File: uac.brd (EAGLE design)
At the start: 100 x 100 mm, 201 parts, among them Q1 2N7002CK4SST, Q6 2N7002CK4SST, Q7 2N7002CK4SST, U2 ADXL345, Y1 RESONATORSMD

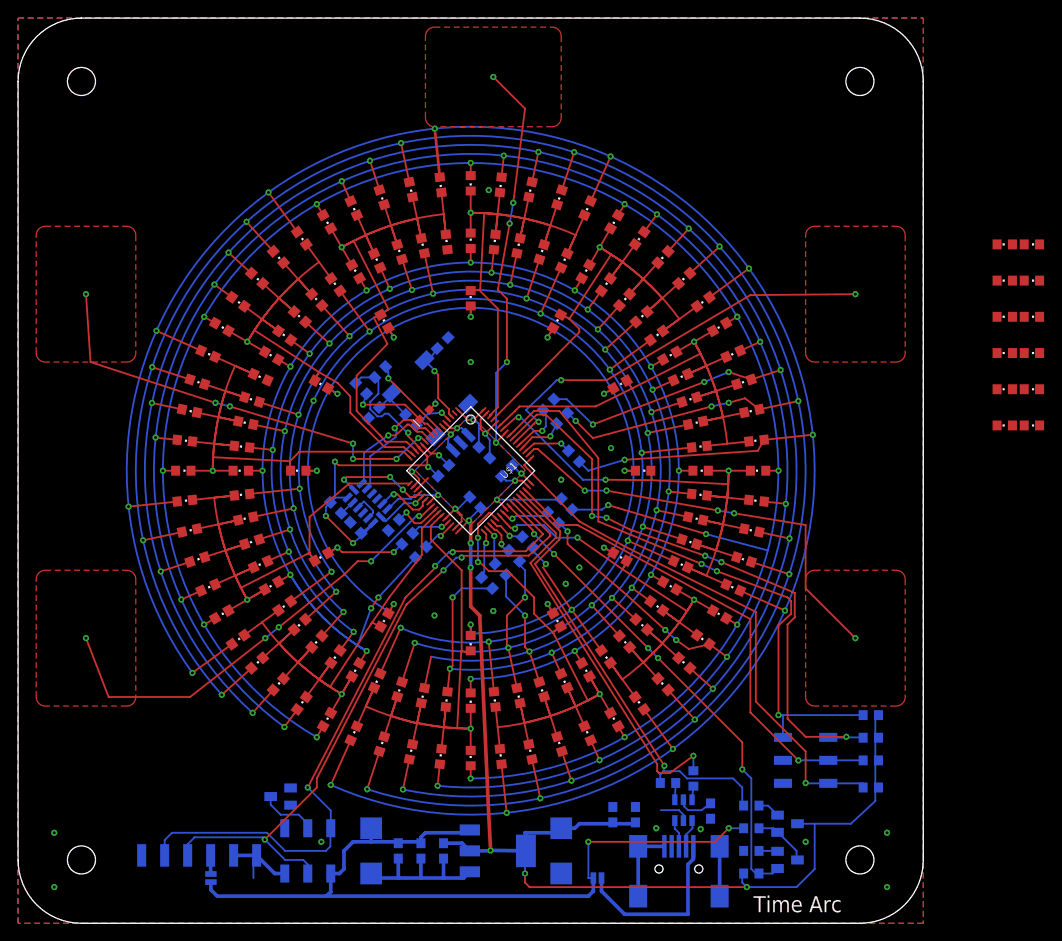
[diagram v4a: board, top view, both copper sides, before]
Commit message: connected wake
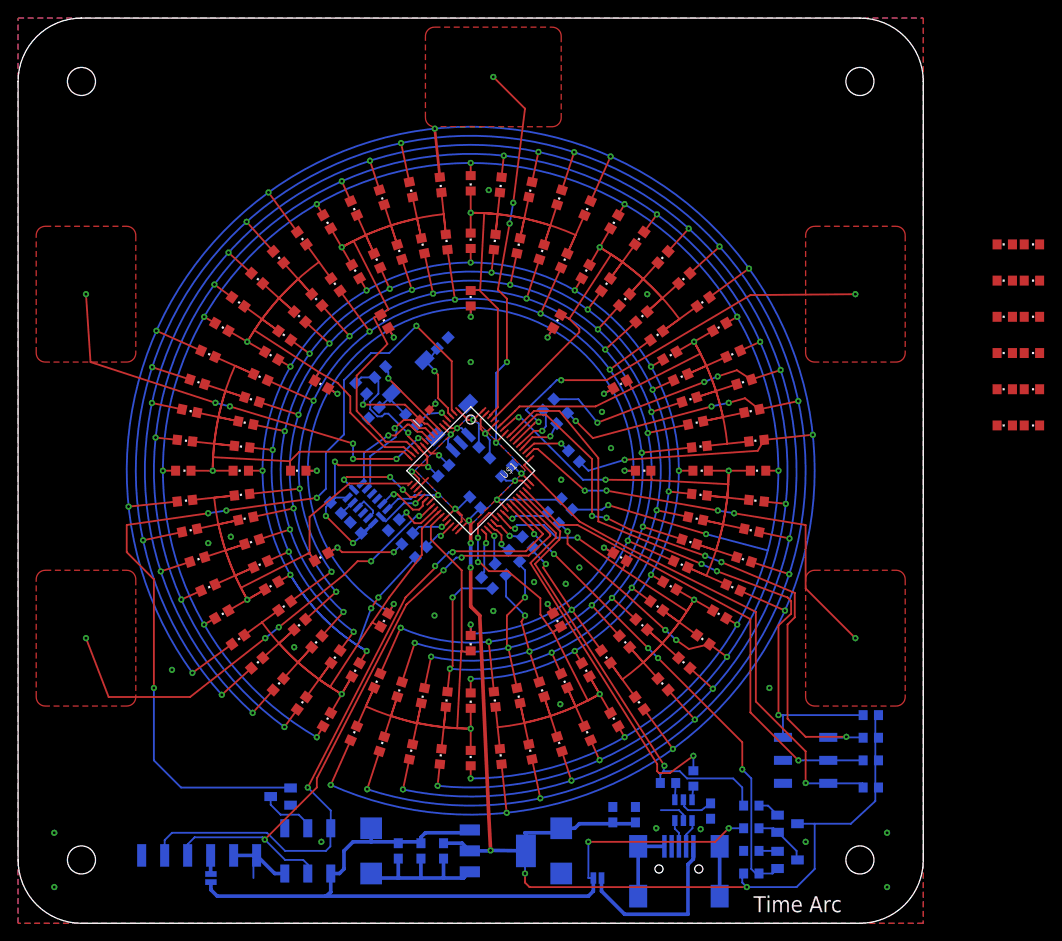
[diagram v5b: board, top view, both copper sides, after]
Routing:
- net WAKE: track 0.00 -> 100.9 mm, vias 0 -> 5
- net DOZEN6: track 73.9 -> 85.1 mm, vias 12 -> 13
- net DOZEN4: vias 12 -> 13
- net GND: vias 22 -> 31
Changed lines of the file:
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@@
 <wire x1="53.90104375" y1="36.09895625" x2="56" y2="34" width="0.2032" layer="16"/>
 <via x="56" y="34" extent="1-16" drill="0.31"/>
-<wire x1="56" y1="34" x2="56" y2="30.51716875" width="0.2032" layer="1"/>
-<wire x1="56" y1="30.51716875" x2="56.489359375" y2="30.027809375" width="0.2032" layer="1"/>
+<wire x1="56" y1="34" x2="55.6" y2="33.31716875" width="0.2032" layer="1"/>
+<wire x1="55.6" y1="33.31716875" x2="56.489359375" y2="30.027809375" width="0.2032" layer="1"/>
+<via x="45.63" y="29.46" extent="1-16" drill="0.31"/>
 <wire x1="69.972190625" y1="56.489359375" x2="64.051740625" y2="65.606040625" width="0" layer="19" extent="1-1"/>
 <wire x1="54.36615" y1="70.5411" x2="64.051740625" y2="65.606040625" width="0" layer="19" extent="1-1"/>
@@
 <wire x1="65.606040625" y1="35.948259375" x2="70.5411" y2="45.63385" width="0" layer="19" extent="1-1"/>
 <wire x1="56" y1="34" x2="65.606040625" y2="35.948259375" width="0" layer="19" extent="16-16"/>
-<wire x1="45.63385" y1="29.4589" x2="56" y2="30.51716875" width="0" layer="19" extent="1-1"/>
-<wire x1="45.633853125" y1="29.4589" x2="45.63385" y2="29.4589" width="0" layer="19" extent="1-16"/>
+<wire x1="45.63" y1="29.46" x2="53.90104375" y2="36.09895625" width="0" layer="19" extent="16-16"/>
+<wire x1="45.63385" y1="29.4589" x2="45.63" y2="29.46" width="0" layer="19" extent="1-1"/>
+<wire x1="45.633853125" y1="29.4589" x2="45.63" y2="29.46" width="0" layer="19" extent="16-16"/>
 <wire x1="34.393959375" y1="64.051740625" x2="43.510640625" y2="69.972190625" width="0" layer="19" extent="1-1"/>
 <wire x1="29.4589" y1="54.36615" x2="34.393959375" y2="64.051740625" width="0" layer="19" extent="1-1"/>
@@
 <wire x1="58" y1="39.3" x2="61" y2="34.7966" width="0.2032" layer="1"/>
 <wire x1="61" y1="34.7966" x2="61.16791875" y2="34.62868125" width="0.2032" layer="1"/>
+<wire x1="47.433834375" y1="74.415515625" x2="48.26" y2="68.9" width="0.2032" layer="1"/>
+<via x="48.26" y="68.9" extent="1-16" drill="0.31"/>
+<wire x1="48.26" y1="68.9" x2="48.1" y2="68.9" width="0.2032" layer="16"/>
+<wire x1="27.57246875" y1="59.985390625" x2="32.642640625" y2="57.728" width="0.2032" layer="1"/>
 <wire x1="57.728" y1="67.357359375" x2="65.37131875" y2="61.16791875" width="0" layer="19" extent="1-1"/>
+<wire x1="48.26" y1="68.9" x2="57.728" y2="67.357359375" width="0" layer="19" extent="1-1"/>
 <wire x1="68.89591875" y1="51.986040625" x2="65.37131875" y2="61.16791875" width="0" layer="19" extent="1-1"/>
 <wire x1="67.357359375" y1="42.272" x2="68.89591875" y2="51.986040625" width="0" layer="19" extent="1-1"/>
@@
 <wire x1="31.10408125" y1="48.013959375" x2="34.62868125" y2="38.83208125" width="0" layer="19" extent="16-16"/>
 <wire x1="32.642640625" y1="57.728" x2="31.10408125" y2="48.013959375" width="0" layer="19" extent="1-1"/>
-<wire x1="27.57246875" y1="59.985390625" x2="32.642640625" y2="57.728" width="0" layer="19" extent="1-1"/>
 <wire x1="38.83208125" y1="65.37131875" x2="32.642640625" y2="57.728" width="0" layer="19" extent="1-1"/>
-<wire x1="47.433834375" y1="74.415515625" x2="57.728" y2="67.357359375" width="0" layer="19" extent="1-1"/>
 </signal>
 <signal name="DOZEN7">
@@
 <via x="61.124609375" y="15.76196875" extent="1-16" drill="0.31"/>
 <wire x1="60.073946875" y1="18.995546875" x2="61.124609375" y2="15.76196875" width="0.2032" layer="1"/>
-<wire x1="59.20104375" y1="57.901040625" x2="60.6" y2="57.9" width="0.2032" layer="16"/>
-<wire x1="60.6" y1="57.9" x2="63.5" y2="55.1" width="0.2032" layer="16"/>
-<via x="63.5" y="55.1" extent="1-16" drill="0.31"/>
-<wire x1="63.5" y1="55.1" x2="75.8" y2="59.8" width="0.2032" layer="1"/>
+<wire x1="59.20104375" y1="57.901040625" x2="61.9" y2="57.9" width="0.2032" layer="16"/>
+<wire x1="61.9" y1="57.9" x2="64" y2="55.3" width="0.2032" layer="16"/>
+<via x="64" y="55.3" extent="1-16" drill="0.31"/>
+<wire x1="64" y1="55.3" x2="75.8" y2="59.8" width="0.2032" layer="1"/>
 <via x="75.8" y="59.8" extent="1-16" drill="0.31"/>
-<wire x1="75.8" y1="59.8" x2="78.5" y2="60.9" width="0.2032" layer="16"/>
-<via x="78.5" y="60.9" extent="1-16" drill="0.31"/>
-<wire x1="78.5" y1="60.9" x2="81.00445" y2="60.073946875" width="0.2032" layer="1"/>
-<wire x1="78.5" y1="60.9" x2="71.81365" y2="74.22651875" width="0" layer="19" extent="1-1"/>
+<wire x1="75.8" y1="59.8" x2="77.29" y2="60.41" width="0.2032" layer="16"/>
+<via x="77.29" y="60.41" extent="1-16" drill="0.31"/>
+<wire x1="77.29" y1="60.41" x2="79.4" y2="61.1" width="0.2032" layer="1"/>
+<wire x1="79.4" y1="61.1" x2="81.00445" y2="60.073946875" width="0.2032" layer="1"/>
+<wire x1="77.29" y1="60.41" x2="71.81365" y2="74.22651875" width="0" layer="19" extent="1-1"/>
 <wire x1="56.777928125" y1="81.887625" x2="71.81365" y2="74.22651875" width="0" layer="19" extent="1-1"/>
 <wire x1="81.887625" y1="43.22206875" x2="81.00445" y2="60.073946875" width="0" layer="19" extent="1-1"/>
@@
 <wire x1="51" y1="39.9" x2="52" y2="38.9" width="0.2032" layer="1"/>
 <wire x1="52" y1="38.9" x2="54.1" y2="38.9" width="0.2032" layer="1"/>
-<wire x1="54.1" y1="38.9" x2="57" y2="36" width="0.2032" layer="1"/>
-<wire x1="57" y1="36" x2="57" y2="34.205475" width="0.2032" layer="1"/>
-<wire x1="57" y1="34.205475" x2="59.13611875" y2="32.06935625" width="0.2032" layer="1"/>
+<wire x1="54.1" y1="38.9" x2="57.7" y2="35.9" width="0.2032" layer="1"/>
+<wire x1="57.7" y1="35.9" x2="57.7" y2="34.105475" width="0.2032" layer="1"/>
+<wire x1="57.7" y1="34.105475" x2="59.13611875" y2="32.06935625" width="0.2032" layer="1"/>
 <wire x1="52.828425" y1="44.696696875" x2="112.85" y2="75" width="0" layer="19" extent="1-1"/>
 </signal>
@@
 <via x="62" y="39.3" extent="1-16" drill="0.31"/>
 <via x="60.5" y="37.5" extent="1-16" drill="0.31"/>
+<via x="83" y="26" extent="1-16" drill="0.31"/>
+<via x="17" y="28" extent="1-16" drill="0.31"/>
+<via x="21" y="42" extent="1-16" drill="0.31"/>
+<via x="23.5" y="42.7" extent="1-16" drill="0.31"/>
+<via x="30.5" y="30.5" extent="1-16" drill="0.31"/>
+<via x="69.5" y="69.5" extent="1-16" drill="0.31"/>
+<via x="64.5" y="56.5" extent="1-16" drill="0.31"/>
+<via x="59.9" y="24.2" extent="1-16" drill="0.31"/>
+<via x="57" y="37.7" extent="1-16" drill="0.31"/>
 <wire x1="39.2" y1="45.6" x2="43.6360375" y2="48.23223125" width="0" layer="19" extent="1-16"/>
-<wire x1="60.5" y1="37.5" x2="52.5" y2="34.5" width="0" layer="19" extent="1-1"/>
+<wire x1="57" y1="37.7" x2="52.5" y2="34.5" width="0" layer="19" extent="1-1"/>
+<wire x1="38.698959375" y1="55.79895625" x2="44.671571875" y2="52.828428125" width="0" layer="19" extent="1-16"/>
 </signal>
 <signal name="+3V3">
@@
 <wire x1="45.39063125" y1="62.207284375" x2="46.298959375" y2="63.49895625" width="0.2032" layer="16"/>
 <wire x1="47.878678125" y1="56.01040625" x2="47.878678125" y2="56.021321875" width="0.2032" layer="1"/>
-<wire x1="47.878678125" y1="56.021321875" x2="47.6" y2="56.3" width="0.2032" layer="1"/>
-<wire x1="47.6" y1="56.3" x2="47.6" y2="56.8" width="0.2032" layer="1"/>
-<wire x1="47.6" y1="56.8" x2="46.4" y2="58" width="0.2032" layer="1"/>
+<wire x1="47.878678125" y1="56.021321875" x2="47.5" y2="56.4" width="0.2032" layer="1"/>
+<wire x1="47.5" y1="56.4" x2="47.5" y2="56.9" width="0.2032" layer="1"/>
+<wire x1="47.5" y1="56.9" x2="46.4" y2="58" width="0.2032" layer="1"/>
 <wire x1="46.4" y1="58" x2="46.4" y2="60.6" width="0.2032" layer="1"/>
 <wire x1="46.4" y1="60.6" x2="46" y2="61" width="0.2032" layer="1"/>
@@
 <contactref element="Q1" pad="1"/>
 <contactref element="U$1" pad="2"/>
-<wire x1="30.1" y1="14.95" x2="48.23223125" y2="56.363959375" width="0" layer="19" extent="1-16"/>
+<wire x1="48.23223125" y1="56.363959375" x2="48.23223125" y2="56.36776875" width="0.2032" layer="1"/>
+<wire x1="48.23223125" y1="56.36776875" x2="47.9" y2="56.7" width="0.2032" layer="1"/>
+<wire x1="47.9" y1="56.7" x2="47.9" y2="62.1" width="0.2032" layer="1"/>
+<wire x1="47.9" y1="62.1" x2="44" y2="66" width="0.2032" layer="1"/>
+<via x="44" y="66" extent="1-16" drill="0.31"/>
+<wire x1="44" y1="66" x2="41" y2="63" width="0.2032" layer="16"/>
+<wire x1="41" y1="63" x2="39" y2="63" width="0.2032" layer="16"/>
+<wire x1="39" y1="63" x2="36" y2="60" width="0.2032" layer="16"/>
+<wire x1="36" y1="60" x2="36" y2="54" width="0.2032" layer="16"/>
+<wire x1="36" y1="54" x2="34" y2="52" width="0.2032" layer="16"/>
+<wire x1="34" y1="52" x2="34" y2="48" width="0.2032" layer="16"/>
+<wire x1="34" y1="48" x2="33" y2="47" width="0.2032" layer="16"/>
+<via x="33" y="47" extent="1-16" drill="0.31"/>
+<wire x1="33" y1="47" x2="23" y2="45.6" width="0.2032" layer="1"/>
+<via x="23" y="45.6" extent="1-16" drill="0.31"/>
+<wire x1="23" y1="45.6" x2="21" y2="45.3" width="0.2032" layer="16"/>
+<via x="21" y="45.3" extent="1-16" drill="0.31"/>
+<wire x1="21" y1="45.3" x2="12" y2="44" width="0.2032" layer="1"/>
+<wire x1="12" y1="44" x2="12" y2="41" width="0.2032" layer="1"/>
+<wire x1="12" y1="41" x2="15" y2="38" width="0.2032" layer="1"/>
+<wire x1="15" y1="38" x2="15" y2="26" width="0.2032" layer="1"/>
+<via x="15" y="26" extent="1-16" drill="0.31"/>
+<wire x1="15" y1="26" x2="15" y2="18" width="0.2032" layer="16"/>
+<wire x1="15" y1="18" x2="18" y2="15" width="0.2032" layer="16"/>
+<wire x1="18" y1="15" x2="30.05" y2="15" width="0.2032" layer="16"/>
+<wire x1="30.05" y1="15" x2="30.1" y2="14.95" width="0.2032" layer="16"/>
 </signal>
 <signal name="TOUCH1">

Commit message: placing specials
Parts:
- moved SPECIAL3 76.7 mm to (33.0, 53.0)
- moved SPECIAL4 76.1 mm to (33.0, 56.0)
- moved SPECIAL5 70.6 mm to (38.5, 59.5), turned to 180 degrees
- moved SPECIAL6 60.7 mm to (51.5, 59.5), turned to 180 degrees
- moved SPECIAL7 58.0 mm to (54.0, 59.5), turned to 180 degrees
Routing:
- net DOZEN7: track 56.9 -> 58.2 mm
- net ARCDOZEN_6: track 85.4 -> 86.6 mm
- net ARCDOZEN_8: track 79.6 -> 80.4 mm
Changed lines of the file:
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@@
 <attribute name="VALUE" x="110" y="69" size="0.8128" layer="27" font="vector" rot="R180"/>
 </element>
-<element name="SPECIAL3" library="Custom components" package="CHIPLED_0603" value="" x="109" y="63" smashed="yes" rot="R90">
-<attribute name="NAME" x="110" y="62" size="0.8128" layer="51" font="vector" rot="R180"/>
-<attribute name="VALUE" x="110" y="65" size="0.8128" layer="27" font="vector" rot="R180"/>
-</element>
-<element name="SPECIAL4" library="Custom components" package="CHIPLED_0603" value="" x="109" y="59" smashed="yes" rot="R90">
-<attribute name="NAME" x="110" y="58" size="0.8128" layer="51" font="vector" rot="R180"/>
-<attribute name="VALUE" x="110" y="61" size="0.8128" layer="27" font="vector" rot="R180"/>
-</element>
-<element name="SPECIAL5" library="Custom components" package="CHIPLED_0603" value="" x="109" y="55" smashed="yes" rot="R90">
-<attribute name="NAME" x="110" y="54" size="0.8128" layer="51" font="vector" rot="R180"/>
-<attribute name="VALUE" x="110" y="57" size="0.8128" layer="27" font="vector" rot="R180"/>
-</element>
-<element name="SPECIAL6" library="Custom components" package="CHIPLED_0603" value="" x="112" y="55" smashed="yes" rot="R270">
-<attribute name="NAME" x="111" y="56" size="0.8128" layer="51" font="vector"/>
-<attribute name="VALUE" x="111" y="53" size="0.8128" layer="27" font="vector"/>
-</element>
-<element name="SPECIAL7" library="Custom components" package="CHIPLED_0603" value="" x="112" y="59" smashed="yes" rot="R270">
-<attribute name="NAME" x="111" y="60" size="0.8128" layer="51" font="vector"/>
-<attribute name="VALUE" x="111" y="57" size="0.8128" layer="27" font="vector"/>
+<element name="SPECIAL3" library="Custom components" package="CHIPLED_0603" value="" x="33" y="53" smashed="yes" rot="R90">
+<attribute name="NAME" x="34" y="52" size="0.8128" layer="51" font="vector" rot="R180"/>
+<attribute name="VALUE" x="34" y="55" size="0.8128" layer="27" font="vector" rot="R180"/>
+</element>
+<element name="SPECIAL4" library="Custom components" package="CHIPLED_0603" value="" x="33" y="56" smashed="yes" rot="R90">
+<attribute name="NAME" x="34" y="55" size="0.8128" layer="51" font="vector" rot="R180"/>
+<attribute name="VALUE" x="34" y="58" size="0.8128" layer="27" font="vector" rot="R180"/>
+</element>
+<element name="SPECIAL5" library="Custom components" package="CHIPLED_0603" value="" x="38.5" y="59.5" smashed="yes" rot="R180">
+<attribute name="NAME" x="39.5" y="60.5" size="0.8128" layer="51" font="vector" rot="R270"/>
+<attribute name="VALUE" x="36.5" y="60.5" size="0.8128" layer="27" font="vector" rot="R270"/>
+</element>
+<element name="SPECIAL6" library="Custom components" package="CHIPLED_0603" value="" x="51.5" y="59.5" smashed="yes" rot="R180">
+<attribute name="NAME" x="52.5" y="60.5" size="0.8128" layer="51" font="vector" rot="R270"/>
+<attribute name="VALUE" x="49.5" y="60.5" size="0.8128" layer="27" font="vector" rot="R270"/>
+</element>
+<element name="SPECIAL7" library="Custom components" package="CHIPLED_0603" value="" x="54" y="59.5" smashed="yes" rot="R180">
+<attribute name="NAME" x="55" y="60.5" size="0.8128" layer="51" font="vector" rot="R270"/>
+<attribute name="VALUE" x="52" y="60.5" size="0.8128" layer="27" font="vector" rot="R270"/>
 </element>
 <element name="SPECIAL8" library="Custom components" package="CHIPLED_0603" value="" x="112" y="63" smashed="yes" rot="R270">
@@
 <via x="76" y="43" extent="1-16" drill="0.31"/>
 <wire x1="76" y1="43" x2="82.8" y2="41.2" width="0.2032" layer="16"/>
+<wire x1="66.3" y1="21.767565625" x2="67" y2="20.6" width="0.2032" layer="1"/>
 <wire x1="78.23243125" y1="66.3" x2="66.3" y2="78.23243125" width="0" layer="19" extent="1-1"/>
 <wire x1="50" y1="82.6" x2="66.3" y2="78.23243125" width="0" layer="19" extent="1-1"/>
@@
 <wire x1="109.85" y1="67" x2="109.85" y2="71" width="0" layer="19" extent="1-1"/>
 <wire x1="111.15" y1="67" x2="109.85" y2="67" width="0" layer="19" extent="1-1"/>
-<wire x1="109.85" y1="63" x2="109.85" y2="67" width="0" layer="19" extent="1-1"/>
-<wire x1="111.15" y1="63" x2="109.85" y2="63" width="0" layer="19" extent="1-1"/>
-<wire x1="109.85" y1="59" x2="109.85" y2="63" width="0" layer="19" extent="1-1"/>
-<wire x1="111.15" y1="59" x2="109.85" y2="59" width="0" layer="19" extent="1-1"/>
-<wire x1="109.85" y1="55" x2="109.85" y2="59" width="0" layer="19" extent="1-1"/>
-<wire x1="111.15" y1="55" x2="109.85" y2="55" width="0" layer="19" extent="1-1"/>
-<wire x1="40.898959375" y1="43.39895625" x2="109.85" y2="55" width="0" layer="19" extent="1-16"/>
+<wire x1="111.15" y1="63" x2="111.15" y2="67" width="0" layer="19" extent="1-1"/>
+<wire x1="54" y1="60.35" x2="109.85" y2="67" width="0" layer="19" extent="1-1"/>
+<wire x1="51.5" y1="60.35" x2="54" y2="60.35" width="0" layer="19" extent="1-1"/>
+<wire x1="38.5" y1="60.35" x2="51.5" y2="60.35" width="0" layer="19" extent="1-1"/>
+<wire x1="33.85" y1="56" x2="38.5" y2="60.35" width="0" layer="19" extent="1-1"/>
+<wire x1="33.85" y1="53" x2="33.85" y2="56" width="0" layer="19" extent="1-1"/>
+<wire x1="40.898959375" y1="43.39895625" x2="33.85" y2="53" width="0" layer="19" extent="1-16"/>
 </signal>
 <signal name="ARCDOZEN_3">
@@
 <wire x1="42.6" y1="52.1" x2="31.080690625" y2="52.1" width="0.2032" layer="1"/>
 <wire x1="31.080690625" y1="52.1" x2="30.027409375" y2="51.04671875" width="0.2032" layer="1"/>
-<wire x1="43.282484375" y1="51.4142125" x2="108.15" y2="63" width="0" layer="19" extent="1-1"/>
+<wire x1="31.080690625" y1="52.1" x2="32.15" y2="53" width="0" layer="19" extent="1-1"/>
 </signal>
 <signal name="ARCDOZEN_5">
@@
 <wire x1="36.7" y1="58.2" x2="35.3" y2="59.7" width="0.2032" layer="1"/>
 <wire x1="35.3" y1="59.7" x2="33.2265875" y2="60.89278125" width="0.2032" layer="1"/>
-<wire x1="43.6360375" y1="51.767765625" x2="108.15" y2="59" width="0" layer="19" extent="1-1"/>
 <wire x1="26.939328125" y1="66.749509375" x2="26.0978875" y2="65.5222125" width="0" layer="19" extent="1-1"/>
 <wire x1="27.26684375" y1="63.125" x2="25.318275" y2="64.25" width="0" layer="19" extent="1-1"/>
+<wire x1="32.15" y1="56" x2="32.766096875" y2="59.95" width="0" layer="19" extent="1-1"/>
 </signal>
 <signal name="ARCDOZEN_6">
@@
 <wire x1="40.6" y1="53.2" x2="40" y2="53.9" width="0.2032" layer="1"/>
 <wire x1="40" y1="53.9" x2="37.4" y2="56.6" width="0.2032" layer="1"/>
-<wire x1="37.4" y1="56.6" x2="37.4" y2="60.5" width="0.2032" layer="1"/>
+<wire x1="37.4" y1="56.6" x2="37.4" y2="58.6" width="0.2032" layer="1"/>
+<wire x1="37.4" y1="58.6" x2="37.4" y2="60.5" width="0.2032" layer="1"/>
 <wire x1="37.4" y1="60.5" x2="40.8" y2="64" width="0.2032" layer="1"/>
 <wire x1="40.8" y1="64" x2="39.3" y2="66.9" width="0.2032" layer="1"/>
 <wire x1="39.3" y1="66.9" x2="40.05" y2="67.2339" width="0.2032" layer="1"/>
-<wire x1="43.989590625" y1="52.12131875" x2="108.15" y2="55" width="0" layer="19" extent="1-1"/>
+<wire x1="38.5" y1="58.65" x2="37.45" y2="58.65" width="0.2032" layer="1"/>
+<wire x1="37.45" y1="58.65" x2="37.4" y2="58.6" width="0.2032" layer="1"/>
 </signal>
 <signal name="ARCDOZEN_7">
@@
 <wire x1="53" y1="57" x2="53" y2="67.89780625" width="0.2032" layer="1"/>
 <wire x1="53" y1="67.89780625" x2="50.933096875" y2="69.964709375" width="0.2032" layer="1"/>
-<wire x1="62.568165625" y1="78.22855625" x2="112.85" y2="55" width="0" layer="19" extent="1-1"/>
+<wire x1="53" y1="57" x2="51.5" y2="58.65" width="0" layer="19" extent="1-1"/>
 </signal>
 <signal name="ARCDOZEN_8">
@@
 <contactref element="U$1" pad="61"/>
 <wire x1="52.474871875" y1="55.656853125" x2="52.574871875" y2="55.774871875" width="0.2032" layer="1"/>
-<wire x1="52.574871875" y1="55.774871875" x2="62" y2="65.3" width="0.2032" layer="1"/>
-<wire x1="62" y1="65.3" x2="62" y2="65.66619375" width="0.2032" layer="1"/>
-<wire x1="62" y1="65.66619375" x2="60.89278125" y2="66.7734125" width="0.2032" layer="1"/>
-<wire x1="74.99861875" y1="68.162575" x2="112.85" y2="59" width="0" layer="19" extent="1-1"/>
+<wire x1="52.574871875" y1="55.774871875" x2="55.6" y2="58.8" width="0.2032" layer="1"/>
+<wire x1="55.6" y1="58.8" x2="55.6" y2="63.6" width="0.2032" layer="1"/>
+<wire x1="55.6" y1="63.6" x2="56" y2="64" width="0.2032" layer="1"/>
+<wire x1="56" y1="64" x2="59.2" y2="64" width="0.2032" layer="1"/>
+<wire x1="59.2" y1="64" x2="59.3" y2="64.06619375" width="0.2032" layer="1"/>
+<wire x1="59.3" y1="64.06619375" x2="60.89278125" y2="66.7734125" width="0.2032" layer="1"/>
+<wire x1="55.6" y1="58.8" x2="54" y2="58.65" width="0" layer="19" extent="1-1"/>
 </signal>
 <signal name="ARCDOZEN_9">
